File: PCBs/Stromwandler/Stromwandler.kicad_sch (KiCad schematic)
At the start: 10 parts, among them IC1 HO10-P_SP33, J1 Conn_02x05_Odd_Even, J4 2X

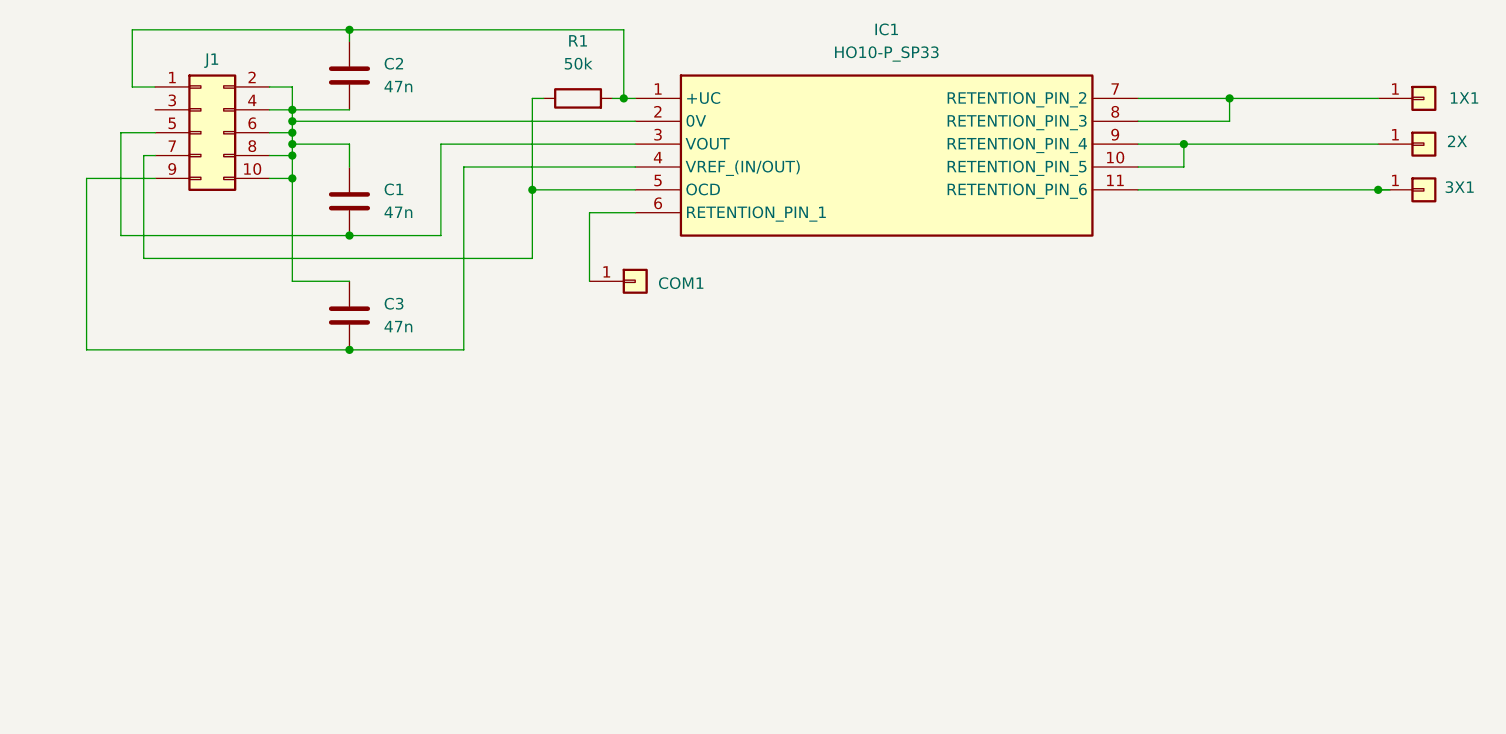
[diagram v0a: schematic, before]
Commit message: Test with smaller holes, bottom only; to avoid DRC errors
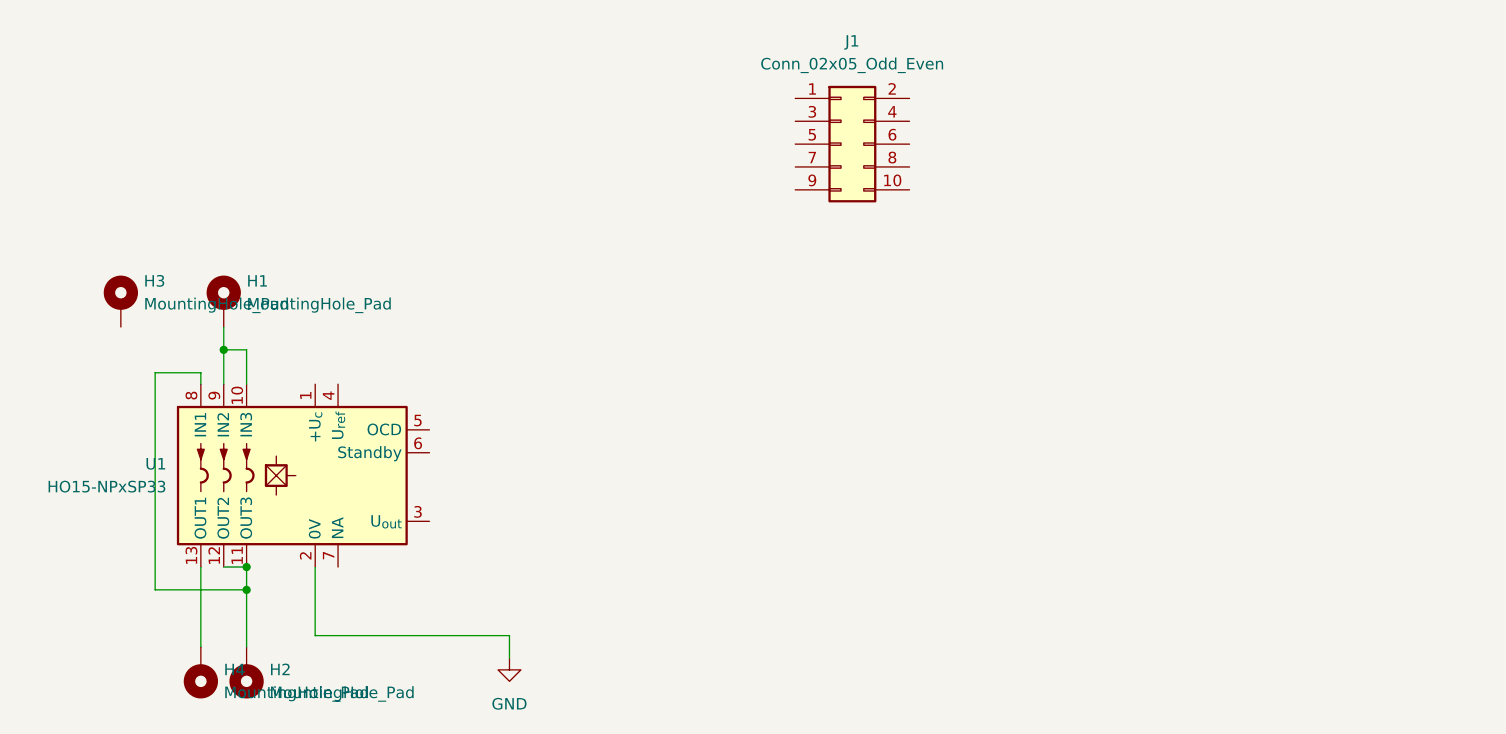
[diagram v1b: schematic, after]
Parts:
- removed 1X1, 3X1, COM1: Conn_01x01, MountingHole:MountingHole_4.3mm_M4_DIN965_Pad, symbol Connector_Generic:Conn_01x01
- removed C1, C2, C3: 47n, Capacitor_SMD:C_0805_2012Metric_Pad1.18x1.45mm_HandSolder, symbol Device:C
- removed IC1: HO10-P_SP33, HO10_P_SP33:HO10PSP33, symbol HO10-P_SP33:HO10-P_SP33
- removed J4: 2X, MountingHole:MountingHole_4.3mm_M4_DIN965_Pad, symbol Connector_Generic:Conn_01x01
- removed R1: 50k, Resistor_SMD:R_0805_2012Metric, symbol Device:R
- added H1, H2, H3, H4: MountingHole_Pad, MountingHole:MountingHole_3.2mm_M3_DIN965_Pad_TopOnly, symbol Mechanical:MountingHole_Pad
- added U1: HO15-NPxSP33, Sensor_Current:LEM_HO8-NP, symbol Sensor_Current:HO15-NPxSP33
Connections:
- new net: H1.1, U1.10 (IN3), U1.9 (IN2)
- new net: H2.1, U1.11 (OUT3), U1.12 (OUT2), U1.8 (IN1)
- new net: H4.1, U1.13 (OUT1)
- new net GND: U1.2 (0V)
- now unconnected: J1.10 (Pin_10), J1.2 (Pin_2), J1.4 (Pin_4), J1.6 (Pin_6), J1.8 (Pin_8)
